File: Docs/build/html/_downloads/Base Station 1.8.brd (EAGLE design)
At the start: 36.8 x 23.5 mm, 21 parts, among them IC1 FT230XS, J1 POWER_JACKPTH, Q1 2222A, U2 TINY85-20-DIP

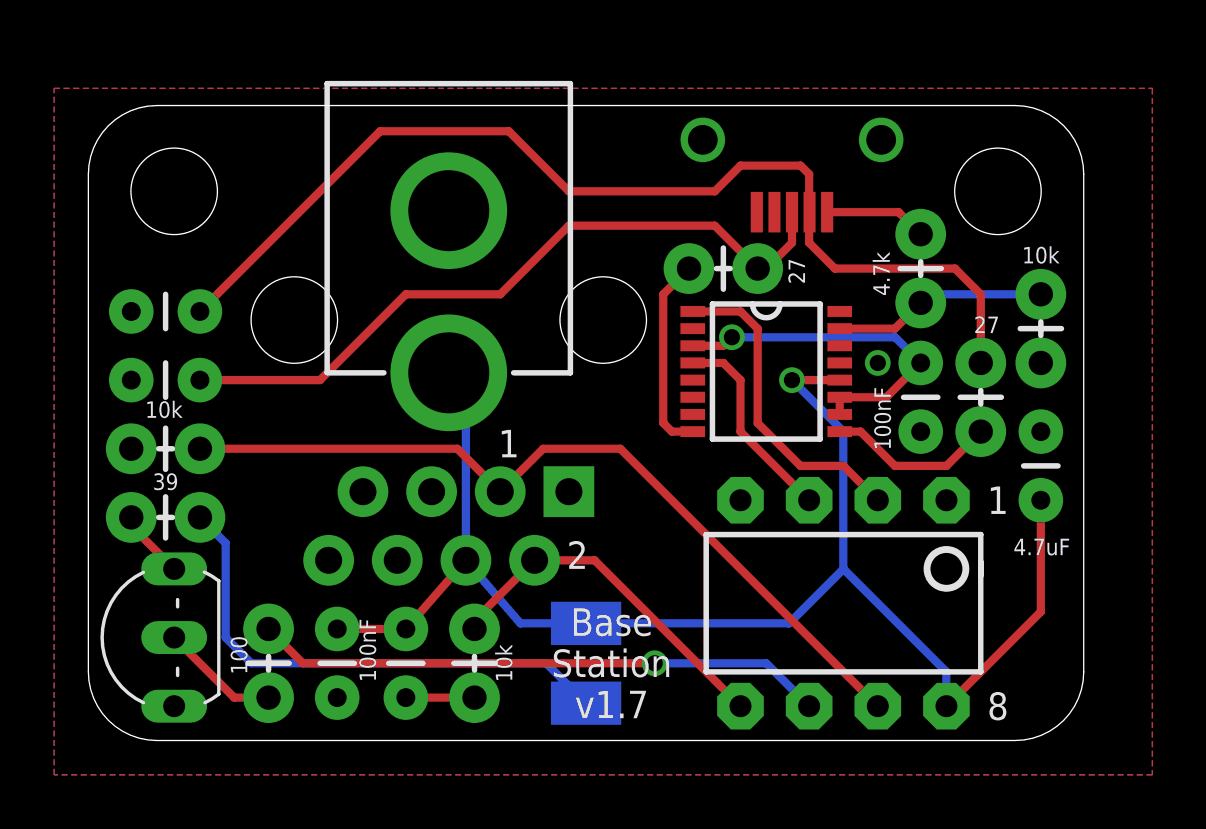
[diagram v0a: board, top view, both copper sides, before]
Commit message: Base station PCB update: Changed to reinforced micro usb for more solid connection. Made 47 pF labels visible. Added OSH logo moved FTDI chip to bottom for easier soldering of the chip and the micro usb Added breakouts for input 1 and input 2.
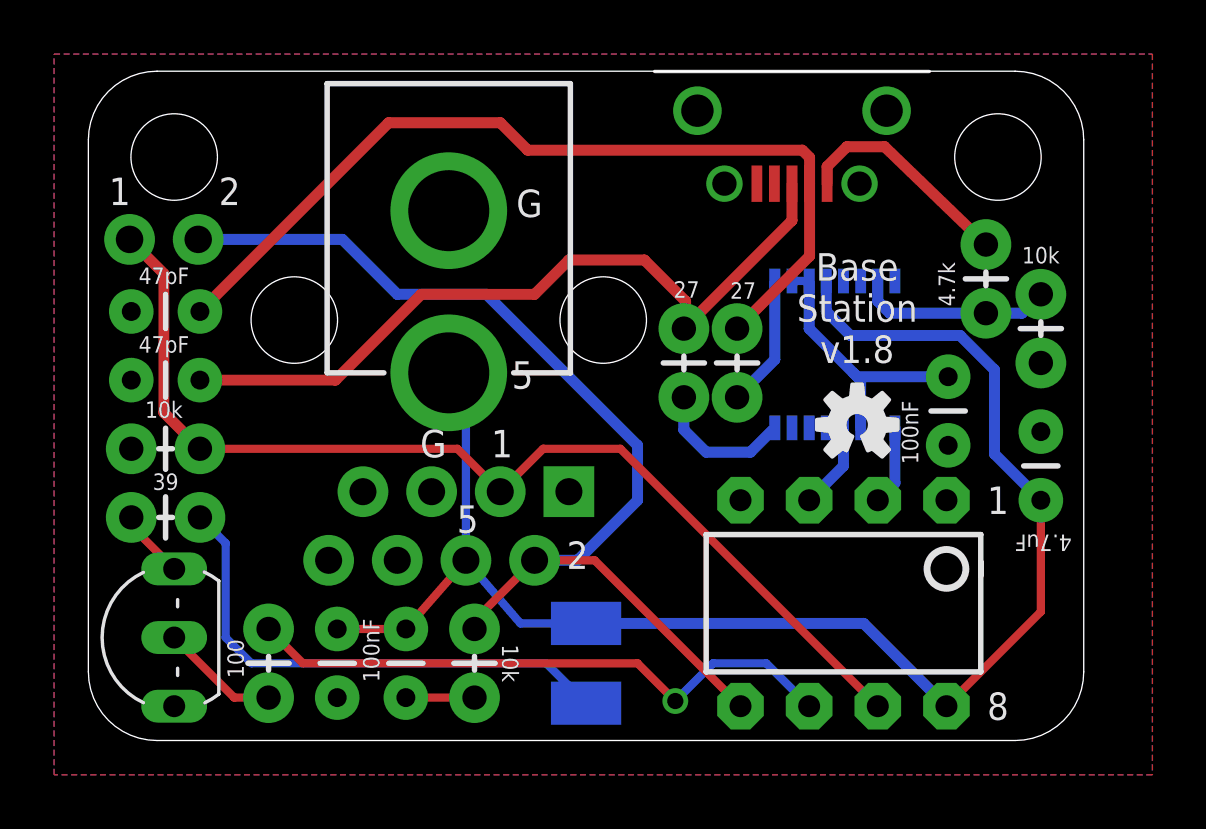
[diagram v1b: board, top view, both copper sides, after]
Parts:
- added JP2: (no value), SparkFun-Connectors:1X02_NO_SILK
- added U$2: (no value), SparkFun-Aesthetics:OSHW-LOGO-S
- added U$4: USB_SOCKET_MICRO_VERTREINFORCED, Andy-library:USB_HORZ_REINFORCED_MICRO
- U$1: value USB_SOCKET_MICRO_VERTHORIZONTAL -> (none); device Andy-library:USB_HORZ_MICRO_SMD -> SparkFun-Aesthetics:OSHW-LOGO-S
- moved U$1 10.8 mm to (28.4, 11.7), turned to 0 degrees
- moved R16 9.11 mm to (24.0, 15.2)
- moved R13 4.77 mm to (22.0, 12.7), turned to 90 degrees
- moved IC1 2.62 mm to (27.6, 14.3), flipped to the bottom, turned to 90 degrees
- moved R14 2.44 mm to (33.2, 15.8)
- moved C7 1.14 mm to (31.8, 13.5)
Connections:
- net GND: now also U$4.G1, U$4.G2, U$4.P$1, U$4.P$2, U$4.P5; no longer U$1.G1, U$1.G2, U$1.P5
- net N$10: now also U$4.P3; no longer U$1.P3
- net N$12: now also U$4.P1; no longer U$1.P1
- net N$9: now also U$4.P2; no longer U$1.P2
- net OUT1: now also JP2.1
- net OUT2: now also JP2.2
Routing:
- net OUT2: track 13.3 -> 39.5 mm
- net 85_RX: track 11.8 -> 2.94 mm
- net OUT1: track 31.2 -> 40.1 mm
- net N$9: track 39.0 -> 33.4 mm
- net N$12: track 3.80 -> 8.28 mm
- net 85_TX: track 7.53 -> 3.21 mm
- net N$16: track 13.1 -> 10.2 mm, vias 1 -> 0
- net N$18: track 7.33 -> 5.29 mm
- net N$10: track 26.5 -> 28.5 mm
- net 5VDC: track 54.3 -> 56.1 mm, vias 1 -> 0
- net N$13: track 6.27 -> 4.88 mm
- net N$4: track 21.2 -> 22.3 mm
- net N$17: track 7.97 -> 7.26 mm
- net GND: vias 1 -> 0
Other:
- board size 36.8 x 23.5 mm -> 36.8 x 24.8 mm
- board text added: "5"
- board text added: "Base Station v1.8"
- board text added: "G"
- board text removed: "Base Station v1.7"
